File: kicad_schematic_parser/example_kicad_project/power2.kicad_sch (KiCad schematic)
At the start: 3 parts, among them U1 NCP1117-3.3_SOT223

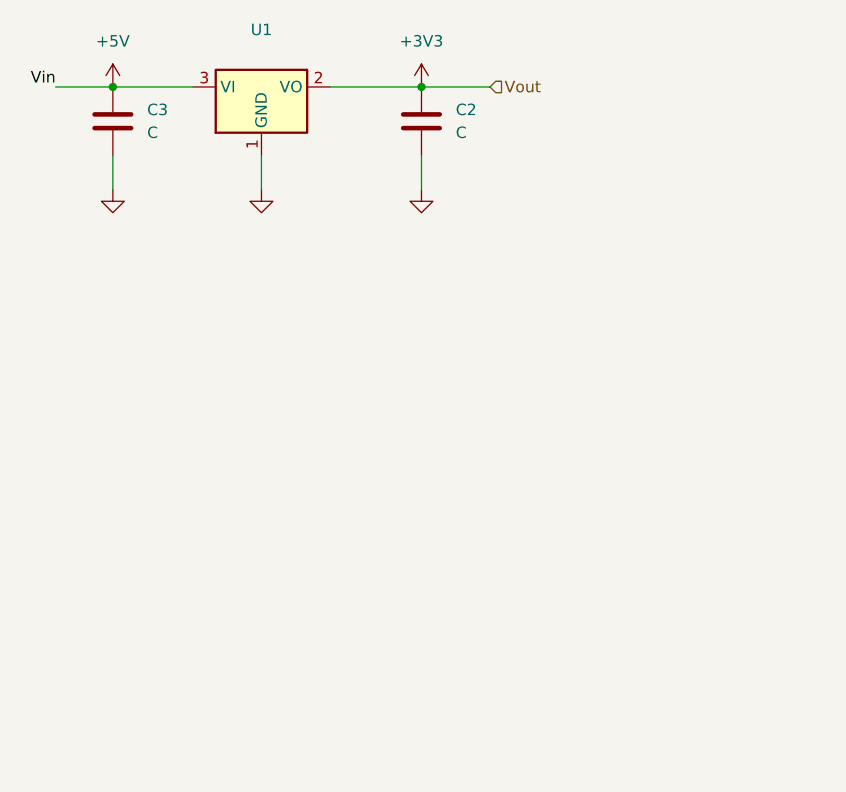
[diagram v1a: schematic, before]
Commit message: change to esp32 project, make more practical
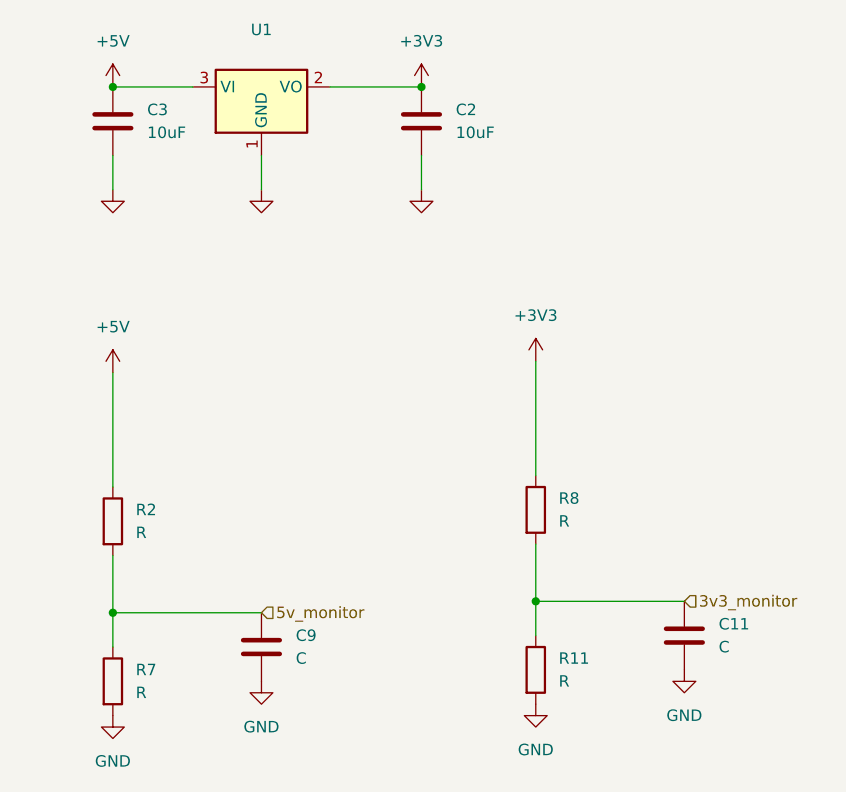
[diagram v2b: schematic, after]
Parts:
- added C11, C9: C, symbol Device:C
- added R11, R2, R7, R8: R, Resistor_SMD:R_0603_1608Metric, symbol Device:R
- C2, C3: value C -> 10uF
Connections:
- net +3V3: now also R8.1
- net +5V: now also R2.1
- net GND: now also C11.2, C9.2, R11.2, R7.2
- new net 3v3_monitor: C11.1, R11.1, R8.2
- new net 5v_monitor: C9.1, R2.2, R7.1
